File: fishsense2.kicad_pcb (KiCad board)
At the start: 2 copper layers, 86.4 x 49.5 mm, 39 parts, among them J1 ORBITTY_EXPANSION, J2 REED_SW, J3 EXT_PWR, J4 V_ORBITTY, J5 V_HUB, J6 PWR_SWITCH, Q1 Q_NMOS_GSD, Q2 Q_PMOS_GDS, U1 TL7702A, U5 P783F-Q24-S5-S

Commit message: Rev 3 Changes
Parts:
- removed G***: LOGO, fishsense2:logo
- added Q3: 2N7002, Package_TO_SOT_SMD:SOT-23, F.Cu at (141.7, 139.2)
- added R11: 50k, Resistor_SMD:R_1206_3216Metric_Pad1.30x1.75mm_HandSolder, F.Cu at (149.4, 137.7)
- added U2: MIC2779L, Package_TO_SOT_SMD:SOT-23-5, F.Cu at (130.6, 138.7)
- C1: value 10n -> 1u
- C2: value 100n -> 1000u; footprint Capacitor_SMD:C_1206_3216Metric_Pad1.33x1.80mm_HandSolder -> Capacitor_THT:CP_Radial_D13.0mm_P5.00mm
- C29: footprint Capacitor_THT:CP_Radial_D5.0mm_P2.00mm -> Capacitor_THT:CP_Radial_D8.0mm_P3.50mm
- C3: value 100n -> 1u
- J1: moved to B.Cu
- R1: value 130 -> 91
- R2: value 50k -> 10M
- R3: value 1M -> 870k
- R4: value 34.8k -> 12k
- R5: value 102k -> 118k
- R7, R8: value 130 -> 150
- U1: value TL7702A -> NCP711; footprint Package_SO:SOIC-8_3.9x4.9mm_P1.27mm -> Package_TO_SOT_SMD:SOT-23-5
- moved R2 43.7 mm to (186.9, 128.5), turned to 90 degrees
- moved C2 32.1 mm to (164.1, 129.5), turned to 0 degrees
- moved R5 19.1 mm to (126.0, 132.1), turned to 90 degrees
- moved R4 17.5 mm to (126.0, 138.2)
- moved R3 17.2 mm to (127.5, 142.7)
- moved C3 16.3 mm to (139.2, 133.1), turned to 0 degrees
- moved C32 16.0 mm to (187.5, 154.4)
- moved C1 9.10 mm to (133.6, 130.6), turned to 0 degrees
- moved U1 3.74 mm to (133.1, 134.1)
- moved R6 2.71 mm to (136.7, 142.7), turned to 0 degrees
- moved J1 2.54 mm to (118.8, 120.9), turned to 180 degrees
- moved C29 1.14 mm to (146.1, 125.9)
- moved TP1 0.13 mm to (147.3, 113.8)
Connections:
- C3 pad 1: Net-(C3-Pad1) -> +3V3
- F1 pad 2: Net-(F1-Pad2) -> Net-(C2-Pad1)
- J1 pad 1: Net-(J1-Pad1) -> unconnected-(J1-Pad1)
- J1 pad 10: Net-(J1-Pad10) -> unconnected-(J1-Pad10)
- J1 pad 11: Net-(J1-Pad11) -> unconnected-(J1-Pad11)
- J1 pad 12: Net-(J1-Pad12) -> unconnected-(J1-Pad12)
- J1 pad 13: Net-(J1-Pad13) -> unconnected-(J1-Pad13)
- J1 pad 14: Net-(J1-Pad14) -> unconnected-(J1-Pad14)
- J1 pad 15: Net-(J1-Pad15) -> unconnected-(J1-Pad15)
- J1 pad 17: Net-(J1-Pad17) -> unconnected-(J1-Pad17)
- J1 pad 2: Net-(J1-Pad2) -> unconnected-(J1-Pad2)
- J1 pad 3: Net-(J1-Pad3) -> unconnected-(J1-Pad3)
- J1 pad 4: Net-(J1-Pad4) -> unconnected-(J1-Pad4)
- J1 pad 5: Net-(J1-Pad5) -> unconnected-(J1-Pad5)
- J1 pad 6: Net-(J1-Pad6) -> unconnected-(J1-Pad6)
- J6 pad 2: Net-(F1-Pad2) -> Net-(C2-Pad1)
- R2 pad 1: /Power/Vext -> Net-(C2-Pad1)
- R2 pad 2: /Power/POWEROFF_OD -> GND
- R3 pad 1: /Power/POWEROFF_OD -> /Power/Vext
- R4 pad 1: /Power/Vext -> Net-(R3-Pad2)
- R4 pad 2: Net-(R3-Pad2) -> Net-(R4-Pad2)
- R5 pad 1: Net-(R3-Pad2) -> Net-(R4-Pad2)
- R6 pad 1: Net-(R6-Pad1) -> Net-(Q3-Pad1)
- U1 pad 1: Net-(C2-Pad1) -> /Power/Vext
- U1 pad 2: /Power/Vext -> GND
- U1 pad 3: Net-(C3-Pad1) -> unconnected-(U1-Pad3)
- U1 pad 4: GND -> unconnected-(U1-Pad4)
- U1 pad 5: /Power/POWEROFF_OD -> +3V3
- U5 pad 1: Net-(U5-Pad1) -> unconnected-(U5-Pad1)
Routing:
- net Net-(C2-Pad1): track 4.17 -> 41.1 mm, vias 0 -> 6
- net Net-(F1-Pad2): track 23.1 -> 0.00 mm
- net Net-(Q3-Pad1): track 0.00 -> 15.5 mm, vias 0 -> 2
- net +3V3: track 0.00 -> 10.2 mm
- net /Power/Vext: track 88.0 -> 98.0 mm
- net /Power/POWEROFF_OD: track 89.5 -> 81.8 mm
- net Net-(C3-Pad1): track 7.64 -> 0.00 mm
- net Net-(J1-Pad7): track 4.63 -> 11.7 mm
- net Net-(R4-Pad2): track 0.00 -> 6.89 mm
- net Net-(R6-Pad1): track 5.64 -> 0.00 mm
- net Net-(J1-Pad9): track 33.4 -> 38.2 mm
- net Net-(R3-Pad2): track 11.1 -> 6.51 mm
- net Net-(J1-Pad8): track 26.7 -> 25.2 mm
- net +5V: track 164.1 -> 165.5 mm
- net GND: vias 8 -> 9
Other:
- net class Default removed
- net class Power removed
- board text added: "Fishsense PIO Rev. 3 SN"
- board text removed: "Fishsense PIO Rev. 2 SN"

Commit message: Some footprint fixes.
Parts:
- Q3: value 2N7002 -> Q_NMOS_GSD; footprint Package_TO_SOT_SMD:SOT-23 -> Package_TO_SOT_SMD:SOT-23_Handsoldering
- moved Q3 0.07 mm to (141.7, 139.1)
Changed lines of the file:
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@@
+    )
+  )
+  (footprint "Package_TO_SOT_SMD:SOT-23_Handsoldering" (layer "F.Cu")
+    (at 141.708 139.126)
+    (descr "SOT-23, Handsoldering")
+    (tags "SOT-23")
+    (property "Sheetfile" "power.kicad_sch")
+    (property "Sheetname" "Power")
+    (attr smd)
+    (fp_text reference "Q3" (at 0 -2.5) (layer "F.SilkS")
+      (effects (font (size 1 1) (thickness 0.15)))
+    )
+    (fp_text value "Q_NMOS_GSD" (at 0 2.5) (layer "F.Fab")
+      (effects (font (size 1 1) (thickness 0.15)))
+    )
+    (fp_text user "${REFERENCE}" (at 0 0 90) (layer "F.Fab")
+      (effects (font (size 0.5 0.5) (thickness 0.075)))
+    )
+    (fp_line (start 0.76 -1.58) (end -2.4 -1.58) (layer "F.SilkS") (width 0.12))
+    (fp_line (start 0.76 -1.58) (end 0.76 -0.65) (layer "F.SilkS") (width 0.12))
+    (fp_line (start 0.76 1.58) (end -0.7 1.58) (layer "F.SilkS") (width 0.12))
+    (fp_line (start 0.76 1.58) (end 0.76 0.65) (layer "F.SilkS") (width 0.12))
+    (fp_line (start -2.7 1.75) (end -2.7 -1.75) (layer "F.CrtYd") (width 0.05))
+    (fp_line (start -2.7 -1.75) (end 2.7 -1.75) (layer "F.CrtYd") (width 0.05))
+    (fp_line (start 2.7 -1.75) (end 2.7 1.75) (layer "F.CrtYd") (width 0.05))
+    (fp_line (start 2.7 1.75) (end -2.7 1.75) (layer "F.CrtYd") (width 0.05))
+    (fp_line (start -0.7 -0.95) (end -0.15 -1.52) (layer "F.Fab") (width 0.1))
+    (fp_line (start -0.15 -1.52) (end 0.7 -1.52) (layer "F.Fab") (width 0.1))
+    (fp_line (start -0.7 -0.95) (end -0.7 1.5) (layer "F.Fab") (width 0.1))
+    (fp_line (start 0.7 -1.52) (end 0.7 1.52) (layer "F.Fab") (width 0.1))
+    (fp_line (start -0.7 1.52) (end 0.7 1.52) (layer "F.Fab") (width 0.1))
+    (pad "1" smd rect (at -1.5 -0.95) (size 1.9 0.8) (layers "F.Cu" "F.Paste" "F.Mask")
+      (net 31 "Net-(Q3-Pad1)") (pinfunction "G") (pintype "input"))
+    (pad "2" smd rect (at -1.5 0.95) (size 1.9 0.8) (layers "F.Cu" "F.Paste" "F.Mask")
+      (net 17 "GND") (pinfunction "S") (pintype "passive"))
+    (pad "3" smd rect (at 1.5 0) (size 1.9 0.8) (layers "F.Cu" "F.Paste" "F.Mask")
+      (net 21 "/Power/POWEROFF_OD") (pinfunction "D") (pintype "passive"))
+    (model "${KICAD6_3DMODEL_DIR}/Package_TO_SOT_SMD.3dshapes/SOT-23.wrl"
+      (offset (xyz 0 0 0))
+      (scale (xyz 1 1 1))
+      (rotate (xyz 0 0 0))
     )
   )
@@
       (offset (xyz 0 0 0))
       (scale (xyz 1 1 1))
-      (rotate (xyz 0 0 0))
-    )
-  )
-  (footprint "Package_TO_SOT_SMD:SOT-23" (layer "F.Cu")
-    (at 141.732 139.192)
-    (descr "SOT, 3 Pin (https://www.jedec.org/system/files/docs/to-236h.pdf variant AB), generated with kicad-footprint-generator ipc_gullwing_generator.py")
-    (tags "SOT TO_SOT_SMD")
-    (property "Sheetfile" "power.kicad_sch")
-    (property "Sheetname" "Power")
-    (attr smd)
-    (fp_text reference "Q3" (at 0 -2.4) (layer "F.SilkS")
-      (effects (font (size 1 1) (thickness 0.15)))
-    )
-    (fp_text value "2N7002" (at 0 2.4) (layer "F.Fab")
-      (effects (font (size 1 1) (thickness 0.15)))
-    )
-    (fp_text user "${REFERENCE}" (at 0 0) (layer "F.Fab")
-      (effects (font (size 0.32 0.32) (thickness 0.05)))
-    )
-    (fp_line (start 0 1.56) (end -0.65 1.56) (layer "F.SilkS") (width 0.12))
-    (fp_line (start 0 -1.56) (end -1.675 -1.56) (layer "F.SilkS") (width 0.12))
-    (fp_line (start 0 1.56) (end 0.65 1.56) (layer "F.SilkS") (width 0.12))
-    (fp_line (start 0 -1.56) (end 0.65 -1.56) (layer "F.SilkS") (width 0.12))
-    (fp_line (start 1.92 -1.7) (end -1.92 -1.7) (layer "F.CrtYd") (width 0.05))
-    (fp_line (start 1.92 1.7) (end 1.92 -1.7) (layer "F.CrtYd") (width 0.05))
-    (fp_line (start -1.92 -1.7) (end -1.92 1.7) (layer "F.CrtYd") (width 0.05))
-    (fp_line (start -1.92 1.7) (end 1.92 1.7) (layer "F.CrtYd") (width 0.05))
-    (fp_line (start -0.65 1.45) (end -0.65 -1.125) (layer "F.Fab") (width 0.1))
-    (fp_line (start 0.65 -1.45) (end 0.65 1.45) (layer "F.Fab") (width 0.1))
-    (fp_line (start -0.65 -1.125) (end -0.325 -1.45) (layer "F.Fab") (width 0.1))
-    (fp_line (start -0.325 -1.45) (end 0.65 -1.45) (layer "F.Fab") (width 0.1))
-    (fp_line (start 0.65 1.45) (end -0.65 1.45) (layer "F.Fab") (width 0.1))
-    (pad "1" smd roundrect (at -0.9375 -0.95) (size 1.475 0.6) (layers "F.Cu" "F.Paste" "F.Mask") (roundrect_rratio 0.25)
-      (net 31 "Net-(Q3-Pad1)") (pinfunction "G") (pintype "input"))
-    (pad "2" smd roundrect (at -0.9375 0.95) (size 1.475 0.6) (layers "F.Cu" "F.Paste" "F.Mask") (roundrect_rratio 0.25)
-      (net 17 "GND") (pinfunction "S") (pintype "passive"))
-    (pad "3" smd roundrect (at 0.9375 0) (size 1.475 0.6) (layers "F.Cu" "F.Paste" "F.Mask") (roundrect_rratio 0.25)
-      (net 21 "/Power/POWEROFF_OD") (pinfunction "D") (pintype "passive"))
-    (model "${KICAD6_3DMODEL_DIR}/Package_TO_SOT_SMD.3dshapes/SOT-23.wrl"
-      (offset (xyz 0 0 0))
-      (scale (xyz 1 1 1))

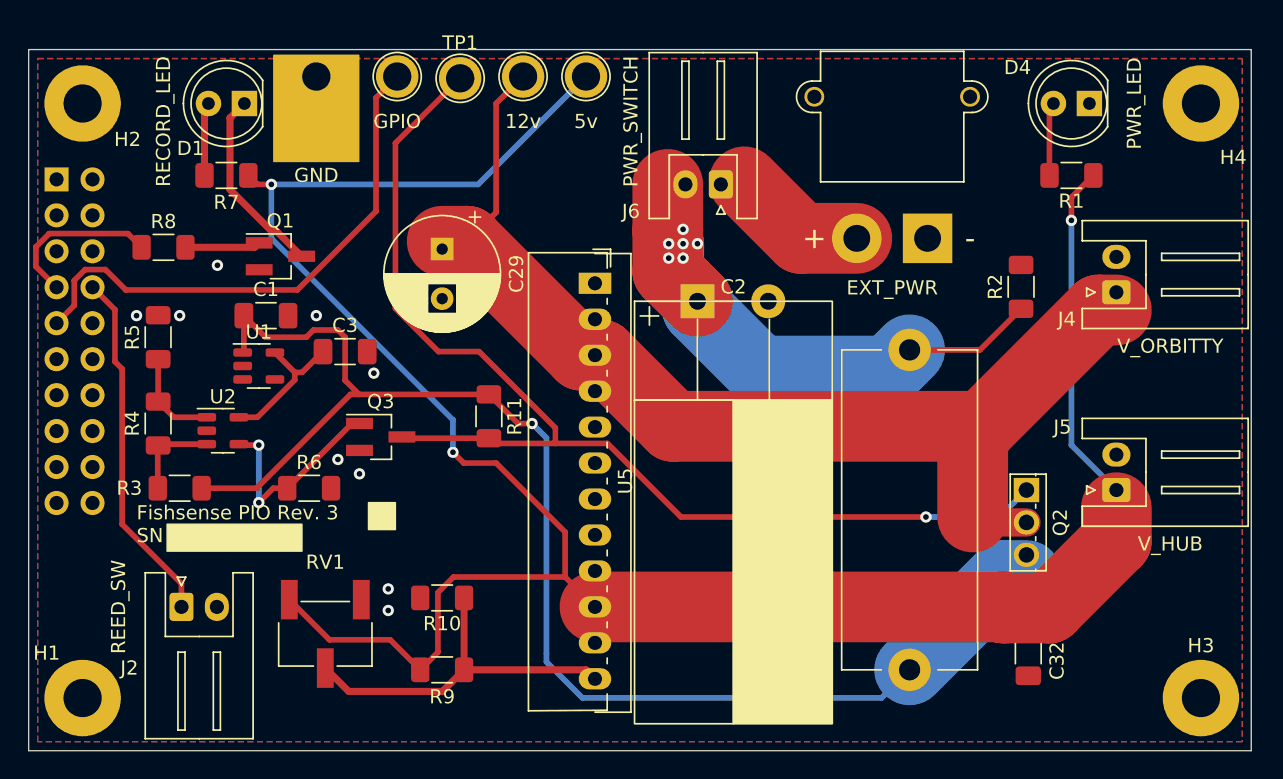
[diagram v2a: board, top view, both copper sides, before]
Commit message: Changed to axial capacitor, fixed mounting hole size.
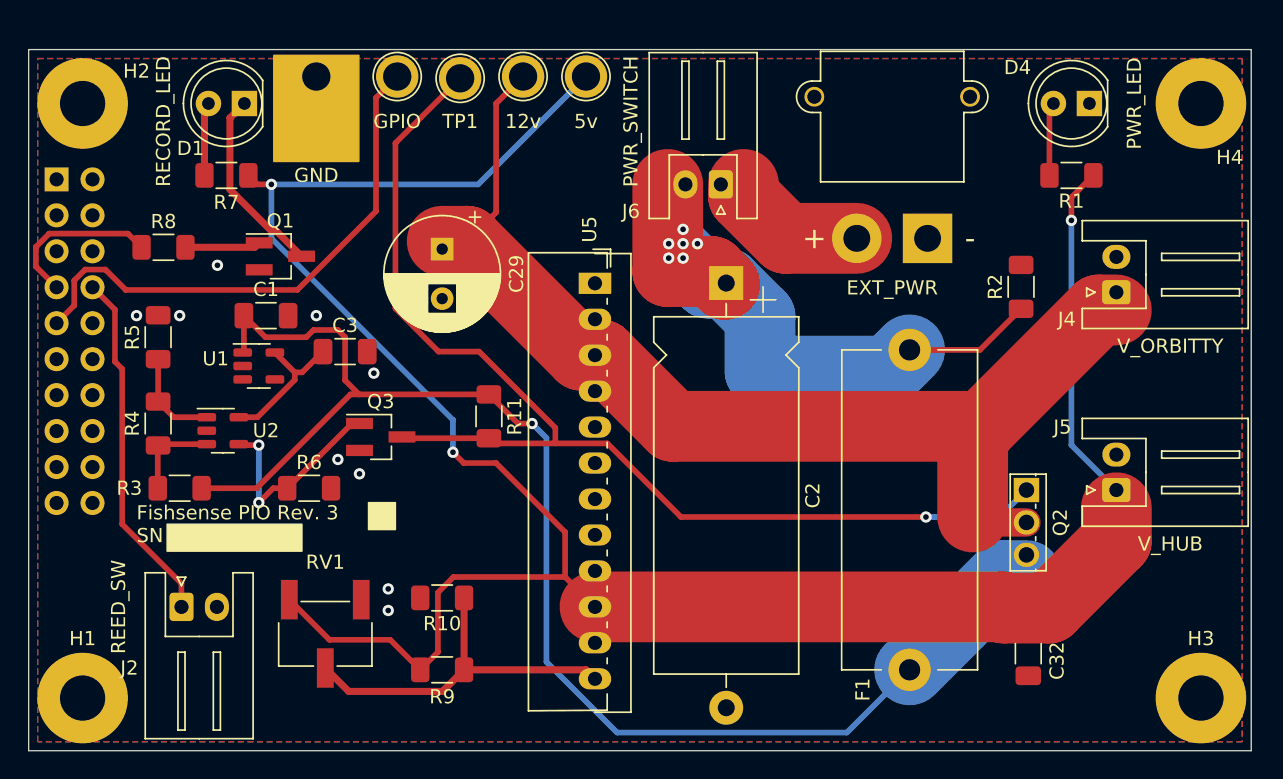
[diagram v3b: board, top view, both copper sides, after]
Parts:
- C2: footprint Capacitor_THT:CP_Radial_D13.0mm_P5.00mm -> Capacitor_THT:CP_Axial_L25.0mm_D10.0mm_P30.00mm_Horizontal
- H1, H2, H3, H4: footprint MountingHole:MountingHole_2.7mm_M2.5_Pad -> MountingHole:MountingHole_3.2mm_M3_Pad
- moved C2 2.40 mm to (166.1, 128.3), turned to -90 degrees
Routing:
- net /Power/Vext: track 98.0 -> 100.1 mm
- net Net-(C2-Pad1): track 41.1 -> 42.5 mm

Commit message: Latest rev 3
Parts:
- moved H1 0.28 mm to (120.7, 157.3)
- moved H3 0.28 mm to (199.7, 157.3)
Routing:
- net GND: track 0.00 -> 1.40 mm, vias 9 -> 10
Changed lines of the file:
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@@
   (net 35 "unconnected-(U5-Pad1)")
   (footprint "MountingHole:MountingHole_3.2mm_M3_Pad" (layer "F.Cu")
-    (at 120.65 157.57)
+    (at 120.65 157.29)
     (descr "Mounting Hole 3.2mm, M3")
     (tags "mounting hole 3.2mm m3")
@@
   )
   (footprint "MountingHole:MountingHole_3.2mm_M3_Pad" (layer "F.Cu")
-    (at 199.65 157.57)
+    (at 199.65 157.29)
     (descr "Mounting Hole 3.2mm, M3")
     (tags "mounting hole 3.2mm m3")
@@
     (fp_line (start -0.711252 0.91) (end 0.711252 0.91) (layer "F.SilkS") (width 0.12))
     (fp_line (start -0.711252 -0.91) (end 0.711252 -0.91) (layer "F.SilkS") (width 0.12))
+    (fp_line (start -2.48 1.15) (end -2.48 -1.15) (layer "F.CrtYd") (width 0.05))
+    (fp_line (start 2.48 -1.15) (end 2.48 1.15) (layer "F.CrtYd") (width 0.05))
     (fp_line (start 2.48 1.15) (end -2.48 1.15) (layer "F.CrtYd") (width 0.05))
-    (fp_line (start -2.48 1.15) (end -2.48 -1.15) (layer "F.CrtYd") (width 0.05))
     (fp_line (start -2.48 -1.15) (end 2.48 -1.15) (layer "F.CrtYd") (width 0.05))
-    (fp_line (start 2.48 -1.15) (end 2.48 1.15) (layer "F.CrtYd") (width 0.05))
+    (fp_line (start -1.6 0.8) (end -1.6 -0.8) (layer "F.Fab") (width 0.1))
     (fp_line (start 1.6 -0.8) (end 1.6 0.8) (layer "F.Fab") (width 0.1))
     (fp_line (start 1.6 0.8) (end -1.6 0.8) (layer "F.Fab") (width 0.1))
     (fp_line (start -1.6 -0.8) (end 1.6 -0.8) (layer "F.Fab") (width 0.1))
-    (fp_line (start -1.6 0.8) (end -1.6 -0.8) (layer "F.Fab") (width 0.1))
     (pad "1" smd roundrect (at -1.5625 0) (size 1.325 1.8) (layers "F.Cu" "F.Paste" "F.Mask") (roundrect_rratio 0.188679)
       (net 26 "/Power/Vext") (pintype "passive"))
@@
   (segment (start 118.292435 124.760489) (end 117.348 125.704924) (width 0.4) (layer "F.Cu") (net 10))
   (segment (start 117.348 125.704924) (end 117.348 127.088) (width 0.4) (layer "F.Cu") (net 10))
+  (segment (start 129.4185 138.684) (end 128.016 138.684) (width 0.5) (layer "F.Cu") (net 17))
   (via (at 130.175 127) (size 0.8) (drill 0.4) (layers "F.Cu" "B.Cu") (net 17))
   (via (at 127.508 130.556) (size 0.8) (drill 0.4) (layers "F.Cu" "B.Cu") (free) (net 17))
   (via (at 140.208 141.732) (size 0.8) (drill 0.4) (layers "F.Cu" "B.Cu") (free) (net 17))
   (via (at 137.16 130.556) (size 0.8) (drill 0.4) (layers "F.Cu" "B.Cu") (free) (net 17))
+  (via (at 128.016 138.684) (size 0.8) (drill 0.4) (layers "F.Cu" "B.Cu") (free) (net 17))
   (via (at 141.224 134.62) (size 0.8) (drill 0.4) (layers "F.Cu" "B.Cu") (free) (net 17))
   (via (at 124.46 130.556) (size 0.8) (drill 0.4) (layers "F.Cu" "B.Cu") (free) (net 17))
